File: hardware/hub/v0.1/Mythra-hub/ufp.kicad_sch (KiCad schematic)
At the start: 12 parts, among them J1 USB_C_Receptacle, U1 TUSB8042A, U2 HD3SS460

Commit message: Re-jigged the hierachy and performed some cleanup
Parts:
- removed U1: TUSB8042A, rhais_package-qfn:QFN-64-1EP_9x9mm_P0.5mm_EP6x6mm, symbol DX-MON:TUSB8042A
- added C8: 0.1uF, rhais_rcl:C0402, symbol Device:C_Small
- J1: value USB_C_Receptacle -> 918-418K2022C40000; MFR (none) -> Jing ext of Electronic Co.; MPN (none) -> 918-418K2022C40000; OC_LCSC (none) -> C168700; URL_LCSC (none) -> https://lcsc.com/product-detail/USB-Connectors_Jing-Extensi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
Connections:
- net +3V3: now also C8.2
- net GND: now also C8.1
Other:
- moved on the sheet: C1, C5, C6, C7, J1, R1, R5, R6, R7, R8, U2

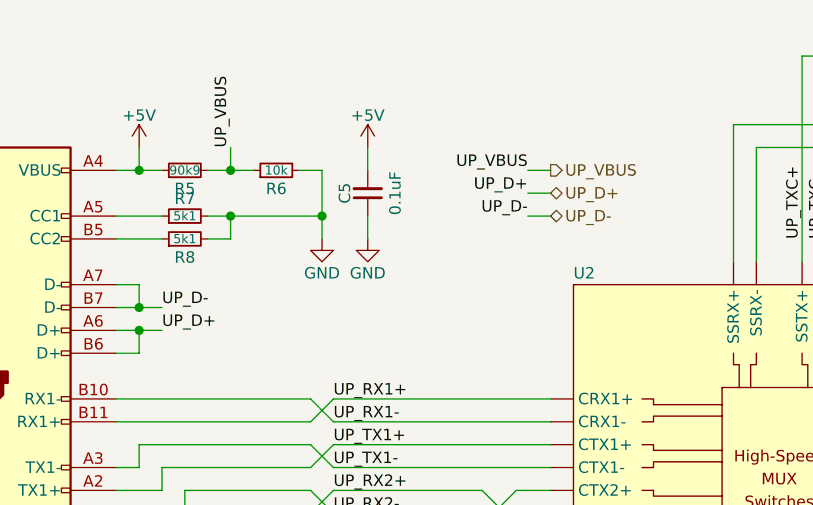
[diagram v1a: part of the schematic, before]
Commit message: Created the DC-DC supply for the hub's core 1.1V rail and added the DFP Type-C recepticals and their shield components
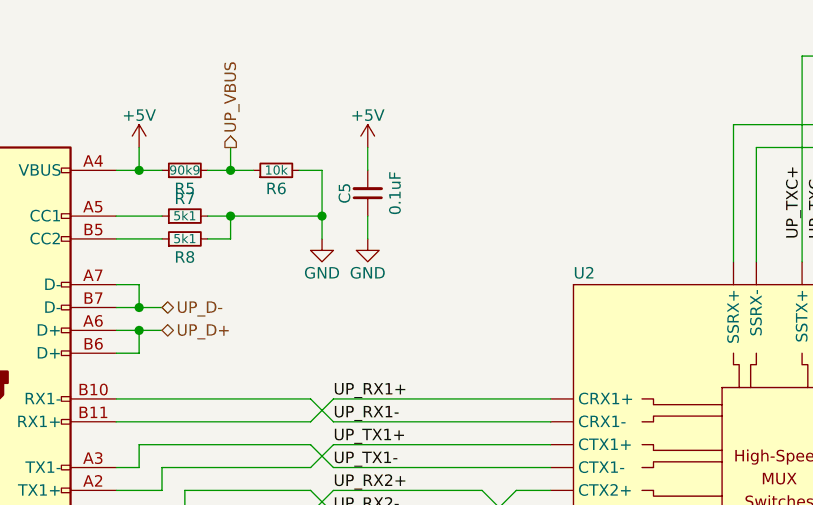
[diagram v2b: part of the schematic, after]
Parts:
- R1: MFR (none) -> Multicomp Pro; MPN (none) -> MCWR04X1004FTL; OC_FARNELL (none) -> 2447127; URL_FARNELL (none) -> https://uk.farnell.com/multicomp/mcwr04x1004ftl/res-1m-1-0-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
- R5: MFR (none) -> Multicomp Pro; MPN (none) -> MCWR04X9092FTL; OC_FARNELL (none) -> 2694669; URL_FARNELL (none) -> https://uk.farnell.com/multicomp/mcwr04x9092ftl/res-90k9-1-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
- R6: MFR (none) -> Yageo; MPN (none) -> RC0402FR-0710KL; OC_LCSC (none) -> C60490; URL_LCSC (none) -> https://lcsc.com/product-detail/Chip-Resistor-Surface-Mount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
- R7, R8: MFR (none) -> Multicomp Pro; MPN (none) -> MCWR04X5101FTL; OC_FARNELL (none) -> 2447201; URL_FARNELL (none) -> https://uk.farnell.com/multicomp/mcwr04x5101ftl/res-5k1-1-0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
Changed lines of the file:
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@@
-    (stroke (width 0) (type solid) (color 0 0 0 0))
-  )
-  (wire (pts (xy 152.4 76.2) (xy 149.86 76.2))
-    (stroke (width 0) (type solid) (color 0 0 0 0))
-  )
-  (wire (pts (xy 152.4 78.74) (xy 149.86 78.74))
-    (stroke (width 0) (type solid) (color 0 0 0 0))
-  )
-  (wire (pts (xy 152.4 81.28) (xy 149.86 81.28))
     (stroke (width 0) (type solid) (color 0 0 0 0))
   )
@@
     (effects (font (size 1.27 1.27)) (justify right bottom))
   )
-  (label "UP_D-" (at 109.22 91.44 0)
-    (effects (font (size 1.27 1.27)) (justify left bottom))
-  )
-  (label "UP_D+" (at 109.22 93.98 0)
-    (effects (font (size 1.27 1.27)) (justify left bottom))
-  )
-  (label "UP_VBUS" (at 116.84 73.66 90)
-    (effects (font (size 1.27 1.27)) (justify left bottom))
-  )
   (label "UP_RX1+" (at 128.27 101.6 0)
     (effects (font (size 1.27 1.27)) (justify left bottom))
@@
     (effects (font (size 1.27 1.27)) (justify left bottom))
   )
-  (label "UP_VBUS" (at 149.86 76.2 180)
-    (effects (font (size 1.27 1.27)) (justify right bottom))
-  )
-  (label "UP_D+" (at 149.86 78.74 180)
-    (effects (font (size 1.27 1.27)) (justify right bottom))
-  )
-  (label "UP_D-" (at 149.86 81.28 180)
-    (effects (font (size 1.27 1.27)) (justify right bottom))
-  )
   (label "UP_TXC+" (at 180.34 83.82 90)
     (effects (font (size 1.27 1.27)) (justify left bottom))
@@
     (effects (font (size 1.27 1.27)) (justify left bottom))
   )
-  (hierarchical_label "UP_VBUS" (shape output) (at 152.4 76.2 0)
-    (effects (font (size 1.27 1.27)) (justify left))
-  )
-  (hierarchical_label "UP_D+" (shape bidirectional) (at 152.4 78.74 0)
-    (effects (font (size 1.27 1.27)) (justify left))
-  )
-  (hierarchical_label "UP_D-" (shape bidirectional) (at 152.4 81.28 0)
+  (hierarchical_label "UP_D-" (shape bidirectional) (at 109.22 91.44 0)
+    (effects (font (size 1.27 1.27)) (justify left))
+  )
+  (hierarchical_label "UP_D+" (shape bidirectional) (at 109.22 93.98 0)
+    (effects (font (size 1.27 1.27)) (justify left))
+  )
+  (hierarchical_label "UP_VBUS" (shape output) (at 116.84 73.66 90)
     (effects (font (size 1.27 1.27)) (justify left))
   )
@@
       (effects (font (size 1.27 1.27)) hide)
     )
-    (property "Datasheet" "~" (id 3) (at 85.09 148.59 0)
+    (property "Datasheet" "https://www.farnell.com/datasheets/2860681.pdf" (id 3) (at 85.09 148.59 0)
+      (effects (font (size 1.27 1.27)) hide)
+    )
+    (property "MFR" "Multicomp Pro" (id 4) (at 85.09 148.59 0)
+      (effects (font (size 1.27 1.27)) hide)
+    )
+    (property "MPN" "MCWR04X1004FTL" (id 5) (at 85.09 148.59 0)
+      (effects (font (size 1.27 1.27)) hide)
+    )
+    (property "OC_FARNELL" "2447127" (id 6) (at 85.09 148.59 0)
+      (effects (font (size 1.27 1.27)) hide)
+    )
+    (property "URL_FARNELL" "https://uk.farnell.com/multicomp/mcwr04x1004ftl/res-1m-1-0-0625w-0402-thick-film/dp/2447127" (id 7) (at 85.09 148.59 0)
       (effects (font (size 1.27 1.27)) hide)
     )
@@
       (effects (font (size 1.27 1.27)) hide)
     )
-    (property "Datasheet" "~" (id 3) (at 111.76 76.2 0)
+    (property "Datasheet" "https://www.farnell.com/datasheets/2189593.pdf" (id 3) (at 111.76 76.2 0)
+      (effects (font (size 1.27 1.27)) hide)
+    )
+    (property "MFR" "Multicomp Pro" (id 4) (at 111.76 76.2 0)
+      (effects (font (size 1.27 1.27)) hide)
+    )
+    (property "MPN" "MCWR04X9092FTL" (id 5) (at 111.76 76.2 0)
+      (effects (font (size 1.27 1.27)) hide)
+    )
+    (property "OC_FARNELL" "2694669" (id 6) (at 111.76 76.2 0)
+      (effects (font (size 1.27 1.27)) hide)
+    )
+    (property "URL_FARNELL" "https://uk.farnell.com/multicomp/mcwr04x9092ftl/res-90k9-1-0-0625w-0402-thick/dp/2694669" (id 7) (at 111.76 76.2 0)
       (effects (font (size 1.27 1.27)) hide)
     )
@@
       (effects (font (size 1.27 1.27)) hide)
     )
-    (property "Datasheet" "~" (id 3) (at 111.76 81.28 0)
+    (property "Datasheet" "https://www.farnell.com/datasheets/2860681.pdf" (id 3) (at 111.76 81.28 0)
+      (effects (font (size 1.27 1.27)) hide)
+    )
+    (property "MFR" "Multicomp Pro" (id 4) (at 111.76 81.28 0)
+      (effects (font (size 1.27 1.27)) hide)
+    )
+    (property "MPN" "MCWR04X5101FTL" (id 5) (at 111.76 81.28 0)
+      (effects (font (size 1.27 1.27)) hide)
+    )
+    (property "OC_FARNELL" "2447201" (id 6) (at 111.76 81.28 0)
+      (effects (font (size 1.27 1.27)) hide)
+    )
+    (property "URL_FARNELL" "https://uk.farnell.com/multicomp/mcwr04x5101ftl/res-5k1-1-0-0625w-thick-film/dp/2447201" (id 7) (at 111.76 81.28 0)
       (effects (font (size 1.27 1.27)) hide)
     )
@@
       (effects (font (size 1.27 1.27)) hide)
     )
-    (property "Datasheet" "~" (id 3) (at 111.76 83.82 0)
+    (property "Datasheet" "https://www.farnell.com/datasheets/2860681.pdf" (id 3) (at 111.76 83.82 0)
+      (effects (font (size 1.27 1.27)) hide)
+    )
+    (property "MFR" "Multicomp Pro" (id 4) (at 111.76 83.82 0)
+      (effects (font (size 1.27 1.27)) hide)
+    )
+    (property "MPN" "MCWR04X5101FTL" (id 5) (at 111.76 83.82 0)
+      (effects (font (size 1.27 1.27)) hide)
+    )
+    (property "OC_FARNELL" "2447201" (id 6) (at 111.76 83.82 0)
+      (effects (font (size 1.27 1.27)) hide)
+    )
+    (property "URL_FARNELL" "https://uk.farnell.com/multicomp/mcwr04x5101ftl/res-5k1-1-0-0625w-thick-film/dp/2447201" (id 7) (at 111.76 83.82 0)
       (effects (font (size 1.27 1.27)) hide)
     )
@@
       (effects (font (size 1.27 1.27)) hide)
     )
-    (property "Datasheet" "~" (id 3) (at 121.92 76.2 0)
-      (effects (font (size 1.27 1.27)) hide)
-    )
+    (property "Datasheet" "https://datasheet.lcsc.com/lcsc/1809301715_YAGEO-RC0402FR-0710KL_C60490.pdf" (id 3) (at 121.92 76.2 0)
+      (effects (font (size 1.27 1.27)) hide)
+    )
+    (property "MFR" "Yageo" (id 4) (at 121.92 76.2 0)
+      (effects (font (size 1.27 1.27)) hide)
+    )
+    (property "MPN" "RC0402FR-0710KL" (id 5) (at 121.92 76.2 0)
+      (effects (font (size 1.27 1.27)) hide)
+    )
+    (property "OC_LCSC" "C60490" (id 6) (at 121.92 76.2 0)
+      (effects (font (size 1.27 1.27)) hide)
+    )
+    (property "URL_LCSC" "https://lcsc.com/product-detail/Chip-Resistor-Surface-Mount_YAGEO-RC0402FR-0710KL_C60490.html" (id 7) (at 121.92 76.2 0)
+      (effects (font (size 1.27 1.27)) hide)
+    )

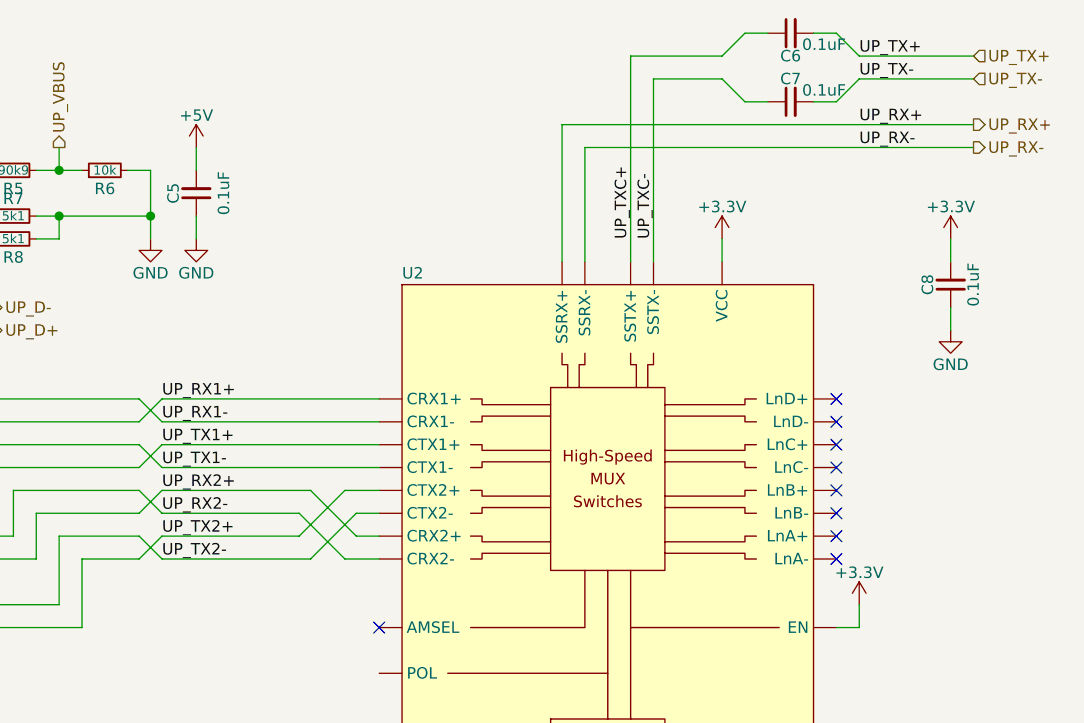
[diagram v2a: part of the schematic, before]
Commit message: Fixed some ERC errors in the UFP schematic and the naming of the superspeed signals
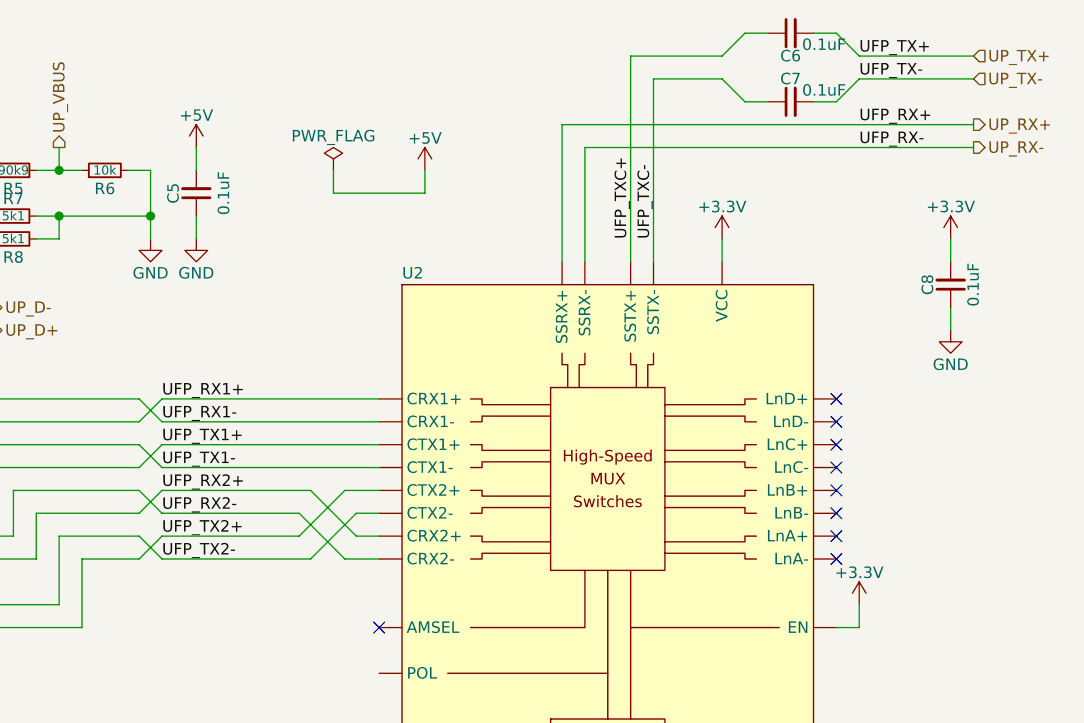
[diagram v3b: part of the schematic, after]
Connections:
- net UP_RX1+ renamed UFP_RX1+
- net UP_RX1- renamed UFP_RX1-
- net UP_RX2+ renamed UFP_RX2+
- net UP_RX2- renamed UFP_RX2-
- net UP_TX1+ renamed UFP_TX1+
- net UP_TX1- renamed UFP_TX1-
- net UP_TX2+ renamed UFP_TX2+
- net UP_TX2- renamed UFP_TX2-
- net UP_TXC+ renamed UFP_TXC+
- net UP_TXC- renamed UFP_TXC-
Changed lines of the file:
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@@
+    (stroke (width 0) (type solid) (color 0 0 0 0))
+  )
+  (wire (pts (xy 147.32 78.74) (xy 147.32 76.2))
     (stroke (width 0) (type solid) (color 0 0 0 0))
   )
@@
   )
   (wire (pts (xy 152.4 119.38) (xy 148.59 119.38))
+    (stroke (width 0) (type solid) (color 0 0 0 0))
+  )
+  (wire (pts (xy 157.48 76.2) (xy 157.48 78.74))
+    (stroke (width 0) (type solid) (color 0 0 0 0))
+  )
+  (wire (pts (xy 157.48 78.74) (xy 147.32 78.74))
     (stroke (width 0) (type solid) (color 0 0 0 0))
   )
@@
     (effects (font (size 1.27 1.27)) (justify right bottom))
   )
-  (label "UP_RX1+" (at 128.27 101.6 0)
-    (effects (font (size 1.27 1.27)) (justify left bottom))
-  )
-  (label "UP_RX1-" (at 128.27 104.14 0)
-    (effects (font (size 1.27 1.27)) (justify left bottom))
-  )
-  (label "UP_TX1+" (at 128.27 106.68 0)
-    (effects (font (size 1.27 1.27)) (justify left bottom))
-  )
-  (label "UP_TX1-" (at 128.27 109.22 0)
-    (effects (font (size 1.27 1.27)) (justify left bottom))
-  )
-  (label "UP_RX2+" (at 128.27 111.76 0)
-    (effects (font (size 1.27 1.27)) (justify left bottom))
-  )
-  (label "UP_RX2-" (at 128.27 114.3 0)
-    (effects (font (size 1.27 1.27)) (justify left bottom))
-  )
-  (label "UP_TX2+" (at 128.27 116.84 0)
-    (effects (font (size 1.27 1.27)) (justify left bottom))
-  )
-  (label "UP_TX2-" (at 128.27 119.38 0)
-    (effects (font (size 1.27 1.27)) (justify left bottom))
-  )
-  (label "UP_TXC+" (at 180.34 83.82 90)
-    (effects (font (size 1.27 1.27)) (justify left bottom))
-  )
-  (label "UP_TXC-" (at 182.88 83.82 90)
-    (effects (font (size 1.27 1.27)) (justify left bottom))
-  )
-  (label "UP_TX+" (at 205.74 63.5 0)
-    (effects (font (size 1.27 1.27)) (justify left bottom))
-  )
-  (label "UP_TX-" (at 205.74 66.04 0)
-    (effects (font (size 1.27 1.27)) (justify left bottom))
-  )
-  (label "UP_RX+" (at 205.74 71.12 0)
-    (effects (font (size 1.27 1.27)) (justify left bottom))
-  )
-  (label "UP_RX-" (at 205.74 73.66 0)
+  (label "UFP_RX1+" (at 128.27 101.6 0)
+    (effects (font (size 1.27 1.27)) (justify left bottom))
+  )
+  (label "UFP_RX1-" (at 128.27 104.14 0)
+    (effects (font (size 1.27 1.27)) (justify left bottom))
+  )
+  (label "UFP_TX1+" (at 128.27 106.68 0)
+    (effects (font (size 1.27 1.27)) (justify left bottom))
+  )
+  (label "UFP_TX1-" (at 128.27 109.22 0)
+    (effects (font (size 1.27 1.27)) (justify left bottom))
+  )
+  (label "UFP_RX2+" (at 128.27 111.76 0)
+    (effects (font (size 1.27 1.27)) (justify left bottom))
+  )
+  (label "UFP_RX2-" (at 128.27 114.3 0)
+    (effects (font (size 1.27 1.27)) (justify left bottom))
+  )
+  (label "UFP_TX2+" (at 128.27 116.84 0)
+    (effects (font (size 1.27 1.27)) (justify left bottom))
+  )
+  (label "UFP_TX2-" (at 128.27 119.38 0)
+    (effects (font (size 1.27 1.27)) (justify left bottom))
+  )
+  (label "UFP_TXC+" (at 180.34 83.82 90)
+    (effects (font (size 1.27 1.27)) (justify left bottom))
+  )
+  (label "UFP_TXC-" (at 182.88 83.82 90)
+    (effects (font (size 1.27 1.27)) (justify left bottom))
+  )
+  (label "UFP_TX+" (at 205.74 63.5 0)
+    (effects (font (size 1.27 1.27)) (justify left bottom))
+  )
+  (label "UFP_TX-" (at 205.74 66.04 0)
+    (effects (font (size 1.27 1.27)) (justify left bottom))
+  )
+  (label "UFP_RX+" (at 205.74 71.12 0)
+    (effects (font (size 1.27 1.27)) (justify left bottom))
+  )
+  (label "UFP_RX-" (at 205.74 73.66 0)
     (effects (font (size 1.27 1.27)) (justify left bottom))
   )
@@
     (pin "1")
   )
+  (symbol (lib_id "power:+5V") (at 157.48 76.2 0) (unit 1)
+    (in_bom yes) (on_board yes)
+    (property "Reference" "#PWR0116" (id 0) (at 157.48 80.01 0)
+      (effects (font (size 1.27 1.27)) hide)
+    )
+    (property "Value" "+5V" (id 1) (at 157.48 72.644 0))
+    (property "Footprint" "" (id 2) (at 157.48 76.2 0)
+      (effects (font (size 1.27 1.27)) hide)
+    )
+    (property "Datasheet" "" (id 3) (at 157.48 76.2 0)
+      (effects (font (size 1.27 1.27)) hide)
+    )
+    (pin "1")
+  )
   (symbol (lib_id "power:+3.3V") (at 190.5 83.82 0) (unit 1)
     (in_bom yes) (on_board yes)
@@
       (effects (font (size 1.27 1.27)) hide)
     )
+    (pin "1")
+  )
+  (symbol (lib_id "power:PWR_FLAG") (at 147.32 76.2 0) (unit 1)
+    (in_bom yes) (on_board yes)
+    (property "Reference" "#FLG0102" (id 0) (at 147.32 74.295 0)
+      (effects (font (size 1.27 1.27)) hide)
+    )
+    (property "Value" "PWR_FLAG" (id 1) (at 147.32 72.39 0))
+    (property "Footprint" "" (id 2) (at 147.32 76.2 0)
+      (effects (font (size 1.27 1.27)) hide)
+    )
+    (property "Datasheet" "~" (id 3) (at 147.32 76.2 0)
+      (effects (font (size 1.27 1.27)) hide)
+    )

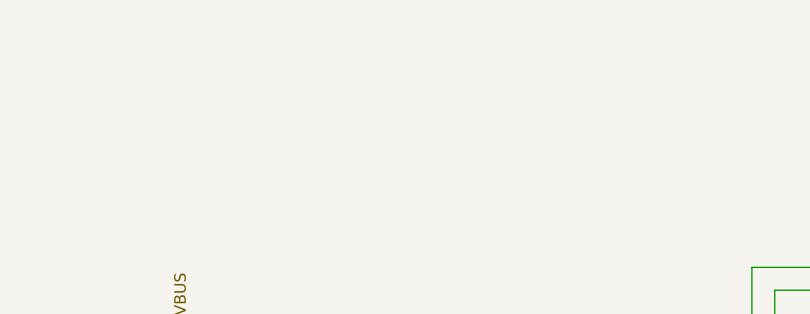
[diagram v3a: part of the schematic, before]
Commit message: Added power delivery control to the DFPs
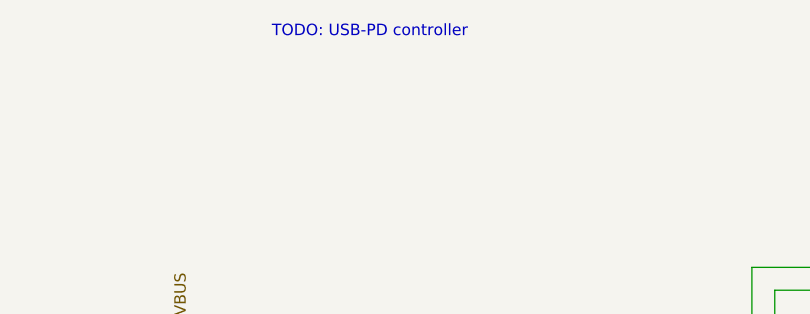
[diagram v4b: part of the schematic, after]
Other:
- note added: "TODO: USB-PD controller"
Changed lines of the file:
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@@
     (stroke (width 0) (type solid) (color 0 0 0 0))
+  )
+  (text "TODO: USB-PD controller" (at 127 38.1 0)
+    (effects (font (size 1.27 1.27)) (justify left bottom))
   )
   (label "UP_SHIELD" (at 81.28 151.13 270)
